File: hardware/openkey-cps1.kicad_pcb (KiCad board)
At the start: 2 copper layers, 108.3 x 80.5 mm, 19 parts, among them J1 CND Top, J2 CNC Top, J3 CNA Top, J4 CNB Top, J5 CND Bottom, J6 CNC Bottom, J7 CNA Bottom, J8 CNB Bottom, J9 Conn_01x03_Female, SW1 SW_DIP_x05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

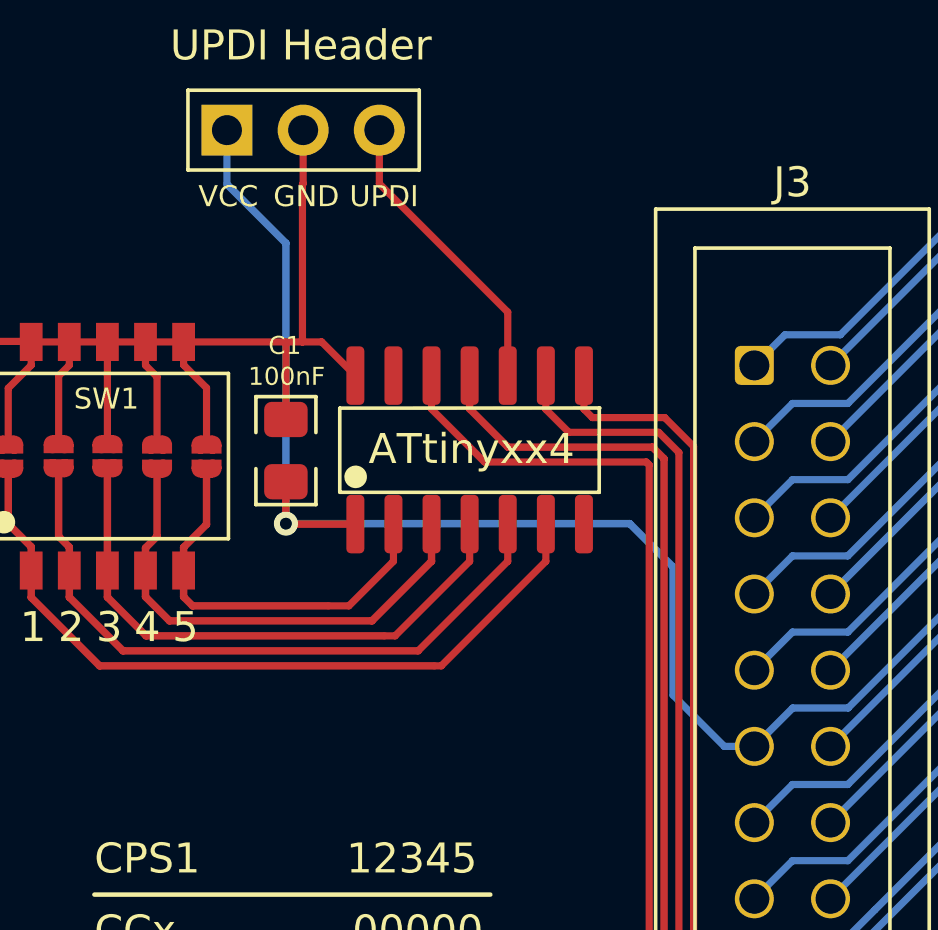
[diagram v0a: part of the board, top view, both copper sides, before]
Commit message: Tweak vcc/gnd traces
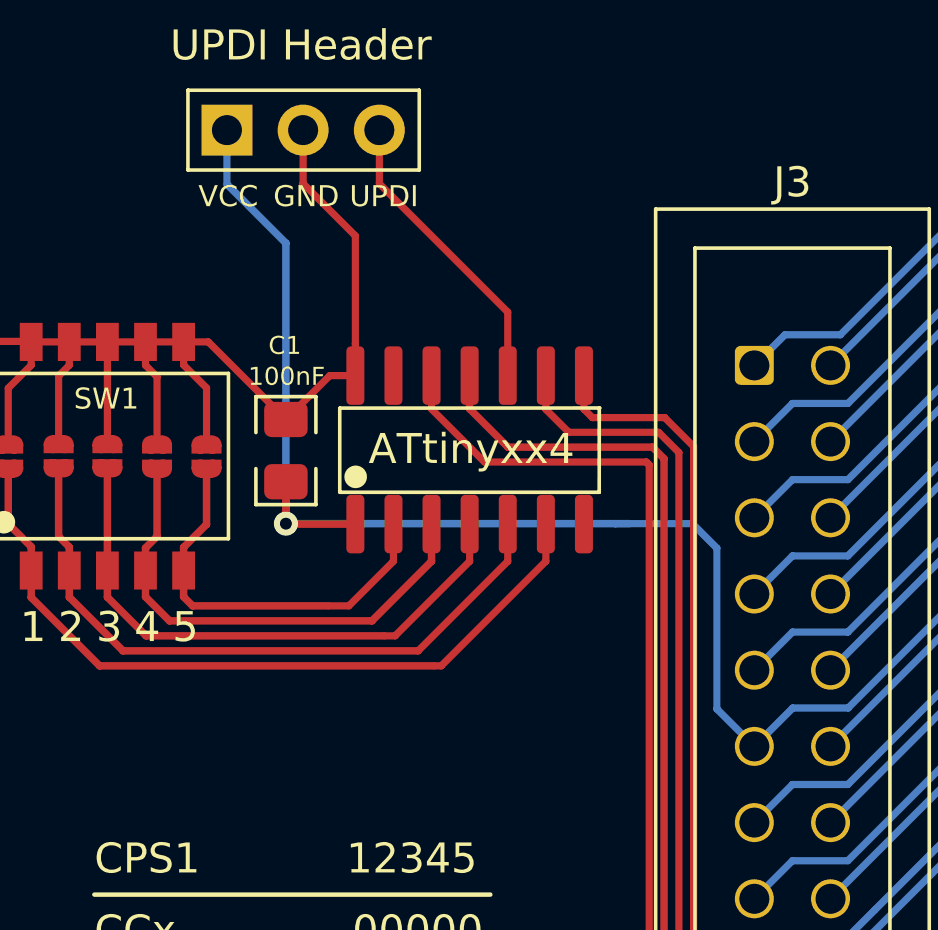
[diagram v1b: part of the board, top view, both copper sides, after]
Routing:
- net VCC: track 63.4 -> 64.5 mm

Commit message: Updated hardware/firmware that adds an optional reset header
The optional reset header that can be used to hookup openkey-cps1
to the A board's reset signal to allow openkey to control it.  In
general you shouldn't need this, but waited to make it an available
option.  More details are in the README.md

The updated firmware is backwards compatible with the previous
hardware revision.
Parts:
- added J11: Conn_01x03_Pin, openkey:PinHeader_1x03_P2.54mm_Vertical, F.Cu at (183.8, 49.6)
- C1: footprint openkey-cps1:C_0805_2012Metric_Pad1.18x1.45mm_HandSolder_alt -> openkey:C_0805_2012Metric_Pad1.18x1.45mm_HandSolder
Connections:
- U1 pad 13: unconnected-(U1-Pad13) -> RESET
- U1 pad 7: unconnected-(U1-Pad7) -> /RESET_DELAY
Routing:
- net GND: track 69.0 -> 25.6 mm
- net /RESET_DELAY: track 0.00 -> 23.2 mm, vias 0 -> 1
- net RESET: track 0.00 -> 22.3 mm, vias 0 -> 1
- net VCC: track 64.5 -> 60.9 mm
- added copper zone on B.Cu, net GND
- added copper zone on F.Cu, net GND
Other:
- board text added: "100nf"
- board text added: "DELAY"
- board text added: "Reset Header (optional)"
- board text added: "TO RESET"
